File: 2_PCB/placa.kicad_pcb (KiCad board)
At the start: 2 copper layers, 38.1 x 95.2 mm, 41 parts, among them J1 Screw_Terminal_01x02, J2 Conn_01x04_Male, J3 Screw_Terminal_01x02, J4 TestPoints, J5 Conn_01x02_Male, U1 STM32L051C8Tx, U2 Ai-Thinker-Ra-01, Y1 8 MHz, Y2 32.768 kHz

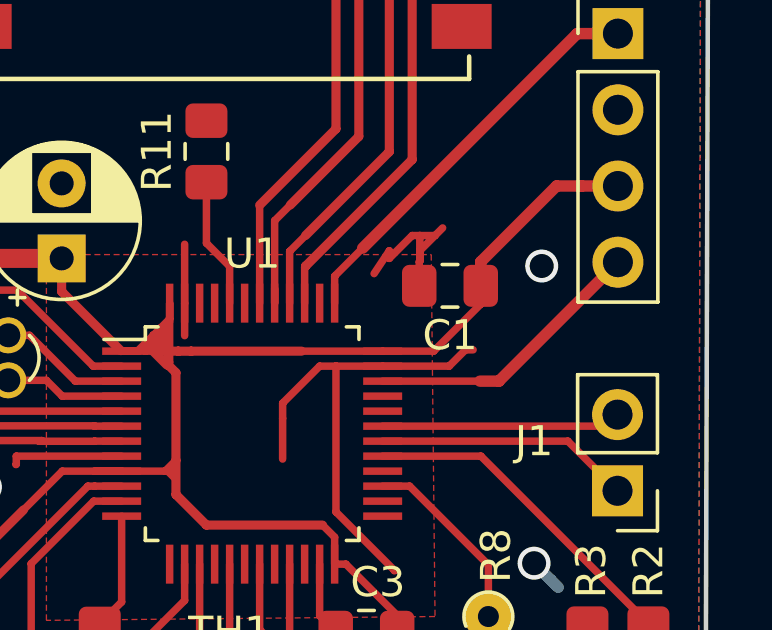
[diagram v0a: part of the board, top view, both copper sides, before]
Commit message: Hardware tested all. MS, HR202, Temperature and LoRa module. Added code for the gateway
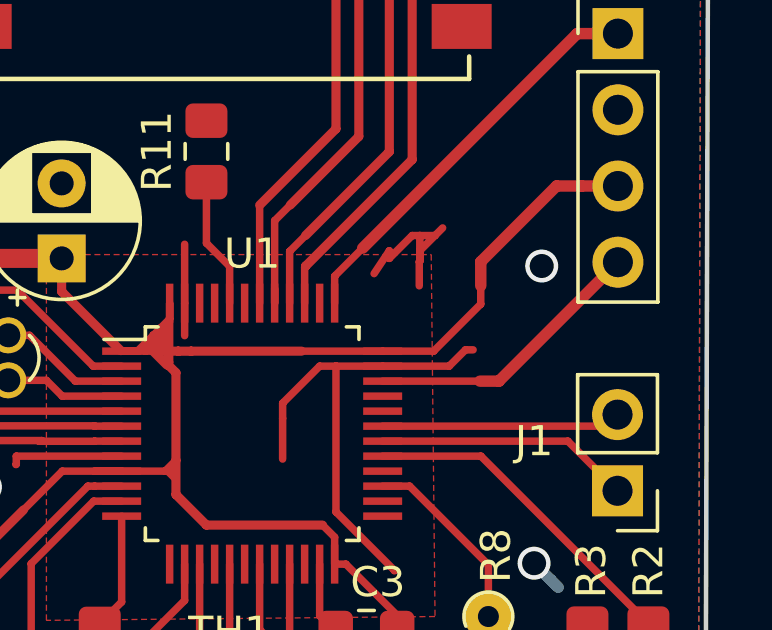
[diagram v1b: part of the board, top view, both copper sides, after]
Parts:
- removed C1: 100n, Capacitor_SMD:C_0805_2012Metric_Pad1.15x1.40mm_HandSolder
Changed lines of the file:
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@@
     (tracks 314)
     (zones 0)
-    (modules 41)
+    (modules 40)
     (nets 32)
   )
@@
     (34 B.Paste user hide)
     (35 F.Paste user hide)
-    (36 B.SilkS user)
-    (37 F.SilkS user)
-    (38 B.Mask user)
-    (39 F.Mask user)
+    (36 B.SilkS user hide)
+    (37 F.SilkS user hide)
+    (38 B.Mask user hide)
+    (39 F.Mask user hide)
     (40 Dwgs.User user hide)
     (41 Cmts.User user hide)
@@
     (44 Edge.Cuts user)
     (45 Margin user hide)
-    (46 B.CrtYd user)
-    (47 F.CrtYd user)
-    (48 B.Fab user)
+    (46 B.CrtYd user hide)
+    (47 F.CrtYd user hide)
+    (48 B.Fab user hide)
     (49 F.Fab user hide)
   )
@@
       (at (xyz 0 0 0))
       (scale (xyz 1 1 1))
-      (rotate (xyz 0 0 0))
-    )
-  )
-  (module Capacitor_SMD:C_0805_2012Metric_Pad1.15x1.40mm_HandSolder (layer F.Cu)
-    (at 133.087 53.2384 180)
-    (descr "Capacitor SMD 0805 (2012 Metric), square (rectangular) end terminal, IPC_7351 nominal with elongated pad for handsoldering. (Body size source: https://docs.google.com/spreadsheets/d/1BsfQQcO9C6DZCsRaXUlFlo91Tg2WpOkGARC1WS5S8t0/edit?usp=sharing), generated with kicad-footprint-generator")
-    (tags "capacitor handsolder")
-    (attr smd)
-    (fp_text reference C1 (at 0 -1.65 180) (layer F.SilkS)
-      (effects (font (size 1 1) (thickness 0.15)))
-    )
-    (fp_text value 100n (at 0 1.65 180) (layer F.Fab)
-      (effects (font (size 1 1) (thickness 0.15)))
-    )
-    (fp_text user %R (at 0.024999 0.034999 180) (layer F.Fab)
-      (effects (font (size 0.5 0.5) (thickness 0.08)))
-    )
-    (fp_line (start 1.85 0.95) (end -1.85 0.95) (layer F.CrtYd) (width 0.05))
-    (fp_line (start 1.85 -0.95) (end 1.85 0.95) (layer F.CrtYd) (width 0.05))
-    (fp_line (start -1.85 -0.95) (end 1.85 -0.95) (layer F.CrtYd) (width 0.05))
-    (fp_line (start -1.85 0.95) (end -1.85 -0.95) (layer F.CrtYd) (width 0.05))
-    (fp_line (start -0.261252 0.71) (end 0.261252 0.71) (layer F.SilkS) (width 0.12))
-    (fp_line (start -0.261252 -0.71) (end 0.261252 -0.71) (layer F.SilkS) (width 0.12))
-    (fp_line (start 1 0.6) (end -1 0.6) (layer F.Fab) (width 0.1))
-    (fp_line (start 1 -0.6) (end 1 0.6) (layer F.Fab) (width 0.1))
-    (fp_line (start -1 -0.6) (end 1 -0.6) (layer F.Fab) (width 0.1))
-    (fp_line (start -1 0.6) (end -1 -0.6) (layer F.Fab) (width 0.1))
-    (pad 2 smd roundrect (at 1.025 0 180) (size 1.15 1.4) (layers F.Cu F.Paste F.Mask) (roundrect_rratio 0.217391)
-      (net 1 GND))
-    (pad 1 smd roundrect (at -1.025 0 180) (size 1.15 1.4) (layers F.Cu F.Paste F.Mask) (roundrect_rratio 0.217391)
-      (net 2 VCC))
-    (model ${KISYS3DMOD}/Capacitor_SMD.3dshapes/C_0805_2012Metric.wrl
-      (at (xyz 0 0 0))
-      (scale (xyz 1 1 1))
